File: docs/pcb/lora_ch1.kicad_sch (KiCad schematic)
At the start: 41 parts

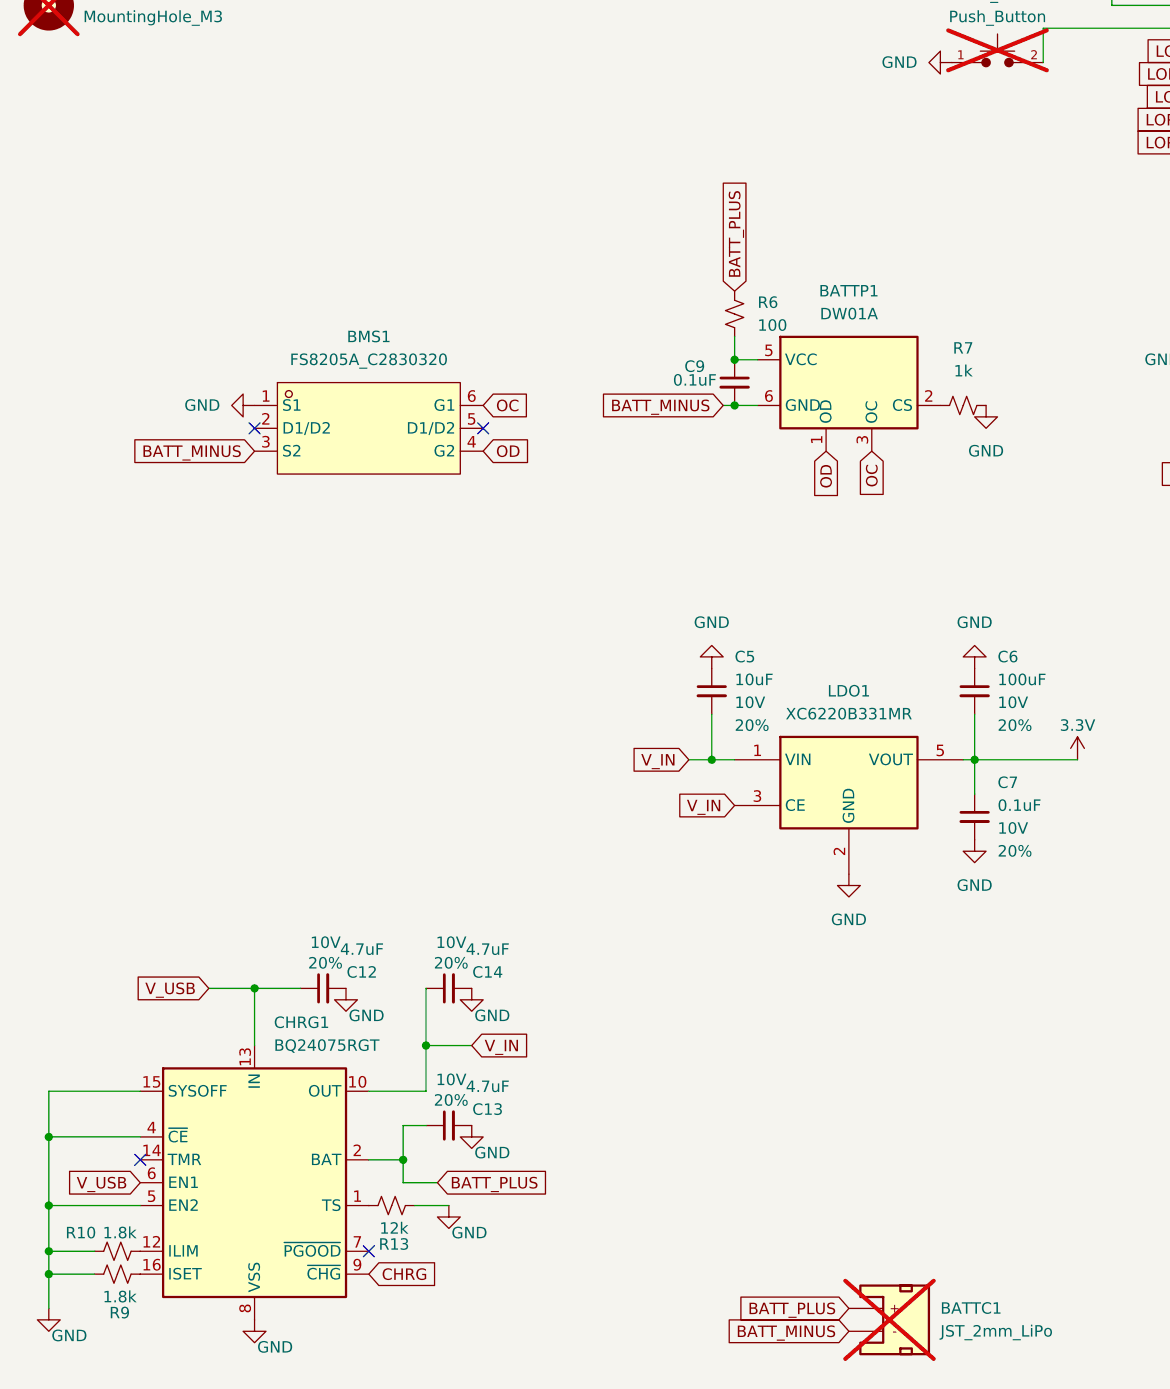
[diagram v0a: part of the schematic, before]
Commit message: PCB rework V1.3 Removed BMS1 (FS8205A), BATTP1 (DW01A) and connected BATT- to GND. Resolved the conflict between battery and built in LDO.
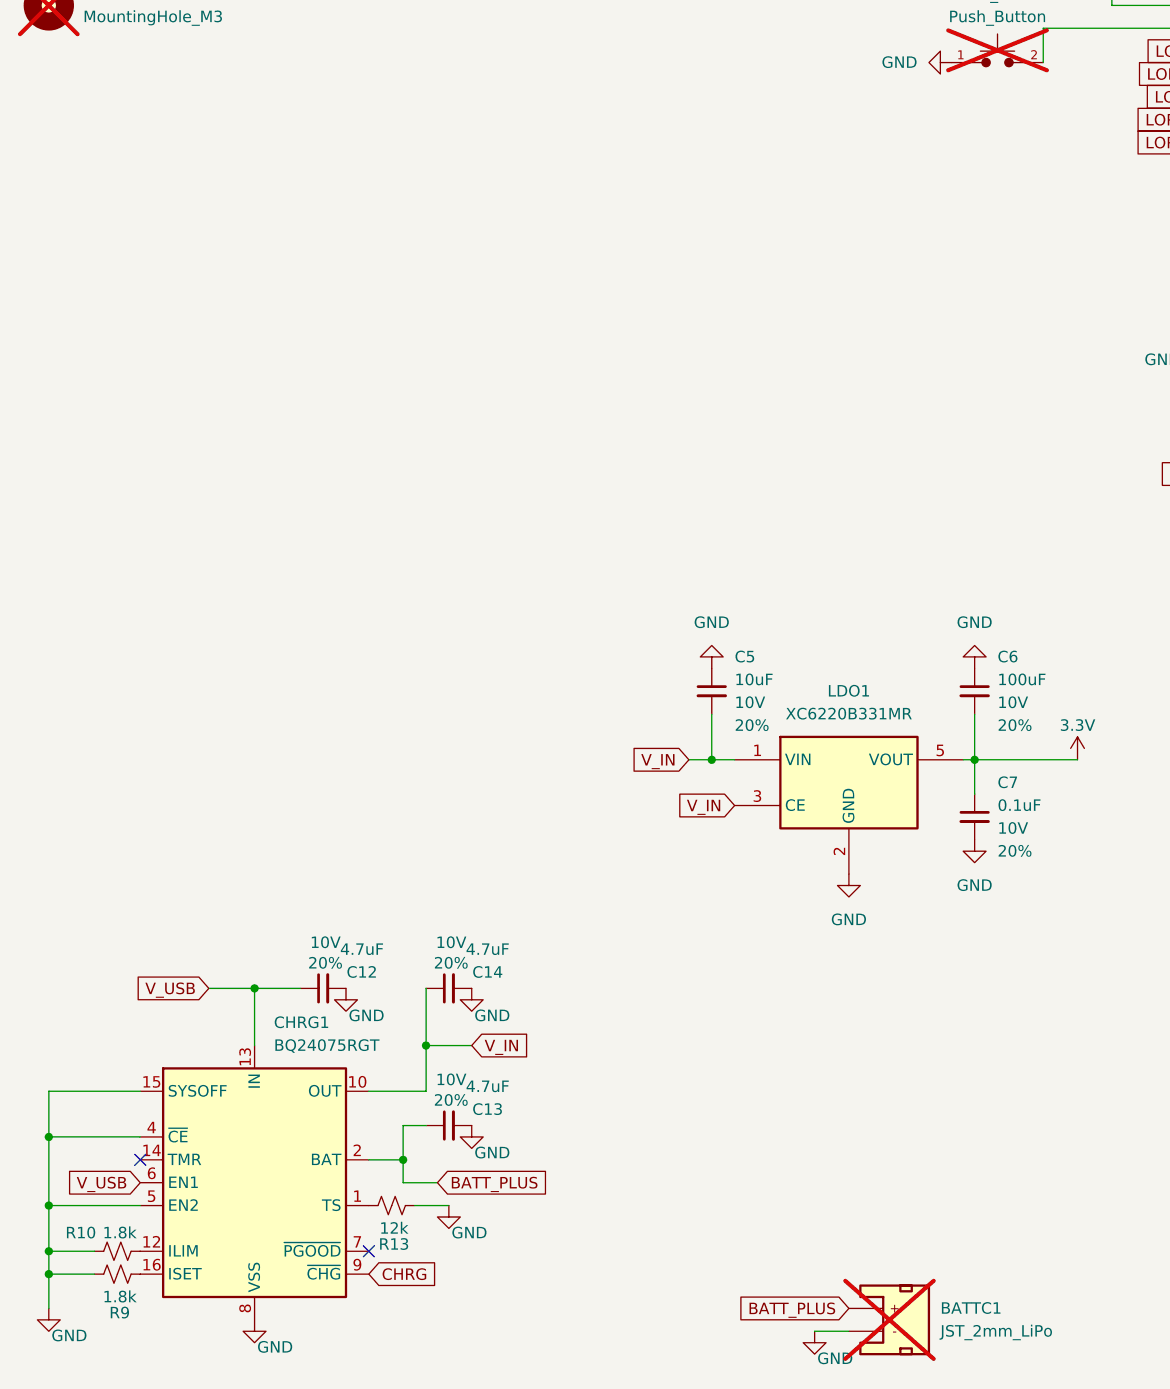
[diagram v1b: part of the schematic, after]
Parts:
- removed BATTP1: DW01A, Package_TO_SOT_SMD:SOT-23-6, symbol Battery_Management:DW01A
- removed BMS1: FS8205A_C2830320, easyeda2kicad:SOT-23-6_L2.9-W1.6-P0.95-LS2.8-BR, symbol FS8205A:FS8205A_C2830320
- removed C9: 0.1uF, PCM_SparkFun-Capacitor:C_0603_1608Metric, symbol PCM_SparkFun-Capacitor:0.1uF_0603_25V_20%
- removed R6: 100, PCM_SparkFun-Resistor:R_0603_1608Metric, symbol PCM_SparkFun-Resistor:100_0603
- removed R7: 1k, PCM_SparkFun-Resistor:R_0603_1608Metric, symbol PCM_SparkFun-Resistor:1k_0603
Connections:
- net BATT_MINUS is gone; now on net GND: BATTC1.1 (-)
- no-connect marks 8 -> 6

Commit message: SET_VIB, GET_VIB added. Editable with control char. write to change the haptics profile.
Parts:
- removed BATTC1: JST_2mm_LiPo, PCM_SparkFun-Connector:JST_1x02_P2.0mm_Horizontal_SMD, symbol PCM_SparkFun-Connector:Conn_01x02_JST_P2.0mm_Horizontal_SMD_LiPo
- added BATT_CONN1: Conn_01x02_Pin, Connector_PinHeader_2.54mm:PinHeader_1x02_P2.54mm_Vertical, symbol Connector:Conn_01x02_Pin
- added SW1: SW_SPDT, Button_Switch_SMD:SW_SPDT_PCM12, symbol Switch:SW_SPDT
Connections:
- net BATT_PLUS: now also BATT_CONN1.2 (Pin_2)
- net GND: now also BATT_CONN1.1 (Pin_1)
- net V_IN: now also SW1.1 (A); no longer C14.1, CHRG1.10 (OUT), CHRG1.11 (OUT)
- new net SYS_PWR: C14.1, CHRG1.10 (OUT), CHRG1.11 (OUT), SW1.2 (B)
- no-connect marks 6 -> 7
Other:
- company: (none) -> Roland Kovacs
- title: (none) -> lora-ch1
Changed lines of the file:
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@@
 	(generator_version "10.0")
 	(paper "A4")
+	(title_block
+		(title "lora-ch1")
+		(date "2026-07-18")
+		(rev "2.0")
+		(company "Roland Kovacs")
+	)
 	(junction
 		(at 17.78 176.53)
@@
 	)
 	(no_connect
+		(at 105.41 161.29)
+	)
+	(no_connect
 		(at 267.97 52.07)
 	)
@@
 		)
 	)
-	(global_label "V_IN"
-		(shape input)
-		(at 64.77 151.13 0)
-		(fields_autoplaced yes)
-		(effects
-			(font
-				(size 1.27 1.27)
-			)
-			(justify left)
-		)
-		(property "Intersheetrefs" "${INTERSHEET_REFS}"
-			(at 71.7467 151.13 0)
-			(hide yes)
-			(show_name no)
-			(do_not_autoplace no)
-			(effects
-				(font
-					(size 1.27 1.27)
-				)
-				(justify left)
-			)
-		)
-	)
 	(global_label "SDA"
 		(shape input)
@@
 		)
 	)
+	(global_label "SYS_PWR"
+		(shape input)
+		(at 64.77 151.13 0)
+		(fields_autoplaced yes)
+		(effects
+			(font
+				(size 1.27 1.27)
+			)
+			(justify left)
+		)
+		(property "Intersheetrefs" "${INTERSHEET_REFS}"
+			(at 76.2218 151.13 0)
+			(hide yes)
+			(show_name no)
+			(do_not_autoplace no)
+			(effects
+				(font
+					(size 1.27 1.27)
+				)
+				(justify left)
+			)
+		)
+	)
 	(global_label "LORA_DIO1"
 		(shape input)
@@
 		)
 	)
+	(global_label "SYS_PWR"
+		(shape input)
+		(at 95.25 158.75 180)
+		(fields_autoplaced yes)
+		(effects
+			(font
+				(size 1.27 1.27)
+			)
+			(justify right)
+		)
+		(property "Intersheetrefs" "${INTERSHEET_REFS}"
+			(at 83.7982 158.75 0)
+			(hide yes)
+			(show_name no)
+			(do_not_autoplace no)
+			(effects
+				(font
+					(size 1.27 1.27)
+				)
+				(justify right)
+			)
+		)
+	)
 	(global_label "SCL"
 		(shape input)
@@
 		)
 	)
+	(global_label "V_IN"
+		(shape input)
+		(at 105.41 156.21 0)
+		(fields_autoplaced yes)
+		(effects
+			(font
+				(size 1.27 1.27)
+			)
+			(justify left)
+		)
+		(property "Intersheetrefs" "${INTERSHEET_REFS}"
+			(at 112.3867 156.21 0)
+			(hide yes)
+			(show_name no)
+			(do_not_autoplace no)
+			(effects
+				(font
+					(size 1.27 1.27)
+				)
+				(justify left)
+			)
+		)
+	)
 	(global_label "LORA_NSS"
 		(shape input)
@@
 	)
 	(symbol
+		(lib_id "Connector:Conn_01x02_Pin")
+		(at 111.76 182.88 180)
+		(unit 1)
+		(body_style 1)
+		(exclude_from_sim no)
+		(in_bom yes)
+		(on_board yes)
+		(in_pos_files yes)
+		(dnp yes)
+		(fields_autoplaced yes)
+		(property "Reference" "BATT_CONN1"
+			(at 113.03 180.3399 0)
+			(show_name no)
+			(do_not_autoplace no)
+			(effects
+				(font
+					(size 1.27 1.27)
+				)
+				(justify right)
+			)
+		)
+		(property "Value" "Conn_01x02_Pin"
+			(at 113.03 182.8799 0)
+			(show_name no)
+			(do_not_autoplace no)
+			(effects
+				(font
+					(size 1.27 1.27)
+				)
+				(justify right)
+			)
+		)
+		(property "Footprint" "Connector_PinHeader_2.54mm:PinHeader_1x02_P2.54mm_Vertical"
+			(at 111.76 182.88 0)
+			(hide yes)
+			(show_name no)
+			(do_not_autoplace no)
+			(effects
+				(font
+					(size 1.27 1.27)
+				)
+			)
+		)
+		(property "Datasheet" ""
+			(at 111.76 182.88 0)
+			(hide yes)
+			(show_name no)
+			(do_not_autoplace no)
+			(effects
+				(font
+					(size 1.27 1.27)
+				)
+			)
+		)
+		(property "Description" "Generic connector, single row, 01x02, script generated"
+			(at 111.76 182.88 0)
+			(hide yes)
+			(show_name no)
+			(do_not_autoplace no)
+			(effects
+				(font
+					(size 1.27 1.27)
+				)
+			)
+		)
+		(pin "1"
+		)
+		(pin "2"
+		)
+		(instances
+			(project "lora_ch1"
+				(path "/796b2641-703b-47b8-9b6b-c931056c1074"
+					(reference "BATT_CONN1")
+					(unit 1)
+				)
+			)
+		)
+	)
+	(symbol
+		(lib_id "Switch:SW_SPDT")
+		(at 100.33 158.75 0)
+		(unit 1)
+		(body_style 1)
+		(exclude_from_sim no)
+		(in_bom yes)
+		(on_board yes)
+		(in_pos_files yes)
+		(dnp yes)
+		(fields_autoplaced yes)
+		(property "Reference" "SW1"
+			(at 100.33 149.86 0)
+			(show_name no)
+			(do_not_autoplace no)
+			(effects
+				(font
+					(size 1.27 1.27)
+				)
+			)
+		)
+		(property "Value" "SW_SPDT"
+			(at 100.33 152.4 0)
+			(show_name no)
+			(do_not_autoplace no)
+			(effects
+				(font
+					(size 1.27 1.27)
+				)
+			)
+		)
+		(property "Footprint" "Button_Switch_SMD:SW_SPDT_PCM12"
+			(at 100.33 158.75 0)
+			(hide yes)
+			(show_name no)
+			(do_not_autoplace no)
+			(effects
+				(font
+					(size 1.27 1.27)
+				)
+			)
+		)
+		(property "Datasheet" ""
+			(at 100.33 166.37 0)
+			(hide yes)
+			(show_name no)
+			(do_not_autoplace no)
+			(effects
+				(font
+					(size 1.27 1.27)
+				)
+			)
+		)
+		(property "Description" "Switch, single pole double throw"
+			(at 100.33 158.75 0)
+			(hide yes)
+			(show_name no)
+			(do_not_autoplace no)
+			(effects
+				(font
+					(size 1.27 1.27)
+				)
+			)
+		)
+		(pin "1"
+		)
+		(pin "2"
+		)
+		(pin "3"
+		)
+		(instances
+			(project "lora_ch1"
+				(path "/796b2641-703b-47b8-9b6b-c931056c1074"
+					(reference "SW1")
+					(unit 1)
+				)
+			)
+		)
+	)
+	(symbol
 		(lib_id "PCM_SparkFun-Capacitor:100uF_1206_50V_10%")
 		(at 120.65 111.76 0)
@@
 					(unit 1)
 				)
-			)
-		)
-	)
-	(symbol
-		(lib_id "PCM_SparkFun-Connector:Conn_01x02_JST_P2.0mm_Horizontal_SMD_LiPo")
-		(at 111.76 180.34 0)
-		(unit 1)
-		(body_style 1)
-		(exclude_from_sim no)
-		(in_bom yes)
-		(on_board yes)
-		(in_pos_files yes)
-		(dnp yes)
-		(fields_autoplaced yes)
-		(property "Reference" "BATTC1"
-			(at 116.84 180.3399 0)
-			(show_name no)
-			(do_not_autoplace no)
-			(effects
-				(font
-					(size 1.27 1.27)
-				)
-				(justify left)
-			)
-		)
-		(property "Value" "JST_2mm_LiPo"
-			(at 116.84 182.8799 0)
-			(show_name no)
-			(do_not_autoplace no)
-			(effects
-				(font
-					(size 1.27 1.27)
-				)
-				(justify left)
-			)
-		)
-		(property "Footprint" "PCM_SparkFun-Connector:JST_1x02_P2.0mm_Horizontal_SMD"
-			(at 111.76 191.77 0)
-			(hide yes)
-			(show_name no)
-			(do_not_autoplace no)
-			(effects
-				(font
-					(size 1.27 1.27)
-				)
-			)
-		)
-		(property "Datasheet" ""
-			(at 111.76 194.31 0)
-			(hide yes)
-			(show_name no)
-			(do_not_autoplace no)
-			(effects
-				(font
-					(size 1.27 1.27)
-				)
-			)
-		)
-		(property "Description" "2 Pin 2mm JST Battery Connector"
-			(at 111.76 199.39 0)
-			(hide yes)
-			(show_name no)
-			(do_not_autoplace no)
-			(effects
-				(font
-					(size 1.27 1.27)
-				)
-			)
-		)
-		(property "PROD_ID" "CONN-11443"
-			(at 111.76 196.85 0)
-			(hide yes)
-			(show_name no)
-			(do_not_autoplace no)
-			(effects
-				(font
-					(size 1.27 1.27)
-				)
-			)
-		)
-		(pin "NC1"
-		)
-		(pin "NC2"
-		)
-		(pin "1"
-		)
-		(pin "2"
-		)
-		(instances
-			(project "lora_ch1"
-				(path "/796b2641-703b-47b8-9b6b-c931056c1074"
-					(reference "BATTC1")
-					(unit 1)
-				)
